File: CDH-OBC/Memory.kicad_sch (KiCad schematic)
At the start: 15 parts, among them U2 MR25H256AMDF, U3 TPS3850H50DRCR, U4 W25N02KVZEIR

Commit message: some progress on kicad
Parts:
- U3: footprint DRC0010J -> OBC-Lib:DRC0010J
- U4: footprint SON_WSON8_ZE_WIN -> OBC-Lib:SON_WSON8_ZE_WIN
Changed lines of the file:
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@@
 			)
 		)
-		(property "Footprint" "DRC0010J"
+		(property "Footprint" "OBC-Lib:DRC0010J"
 			(at 144.78 50.8 0)
 			(hide yes)
@@
 			)
 		)
-		(property "Footprint" "SON_WSON8_ZE_WIN"
+		(property "Footprint" "OBC-Lib:SON_WSON8_ZE_WIN"
 			(at 20.32 95.25 0)
 			(hide yes)

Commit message: changes on rtc
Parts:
- added 1: TL3315NF250Q, symbol OBC-lib:TL3315NF250Q
- added C7: 6.8uF, Capacitor_SMD:C_0603_1608Metric, symbol Device:C_Small
- added C8: 100nF, Capacitor_SMD:C_0603_1608Metric, symbol Device:C_Small
- added C9: 1nF, Capacitor_SMD:C_0603_1608Metric, symbol Device:C_Small
- added R6, R7: 10k, Resistor_SMD:R_0603_1608Metric, symbol Device:R_Small_US
- added U5: PCA2129T/Q900/2_51, SO16_SOT162-1_NXP, symbol OBC-lib:PCA2129T_Q900_2_51
- U3: footprint OBC-Lib:DRC0010J -> DRC0010J
- U4: footprint OBC-Lib:SON_WSON8_ZE_WIN -> SON_WSON8_ZE_WIN
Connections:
- net +3V3: now also C7.2, C8.2, R6.2, U5.16 (VDD)
- net GND: now also C7.1, C8.1, C9.2, U5.15 (VBAT), U5.5 (IFS), U5.8 (VSS)
- new net: R6.1, U5.13 (*INT)
- new net: C9.1, U5.6 (*TS)
- new net: 1.1, 1.2
- new net: 1.3, 1.4

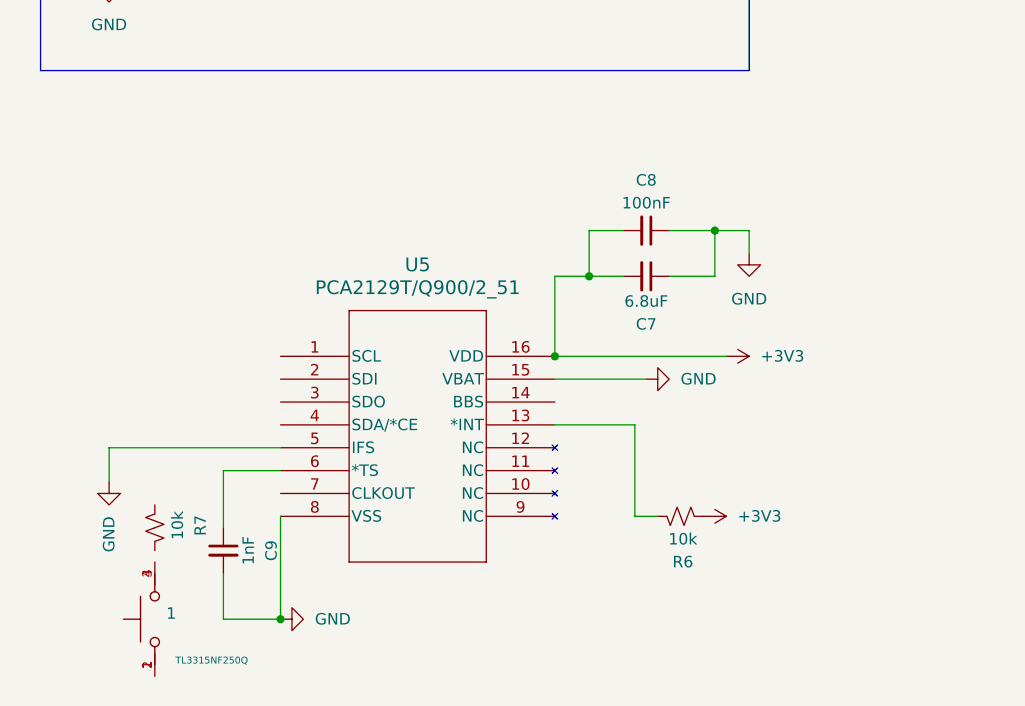
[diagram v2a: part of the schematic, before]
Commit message: changes on mcu and cristal oscillator
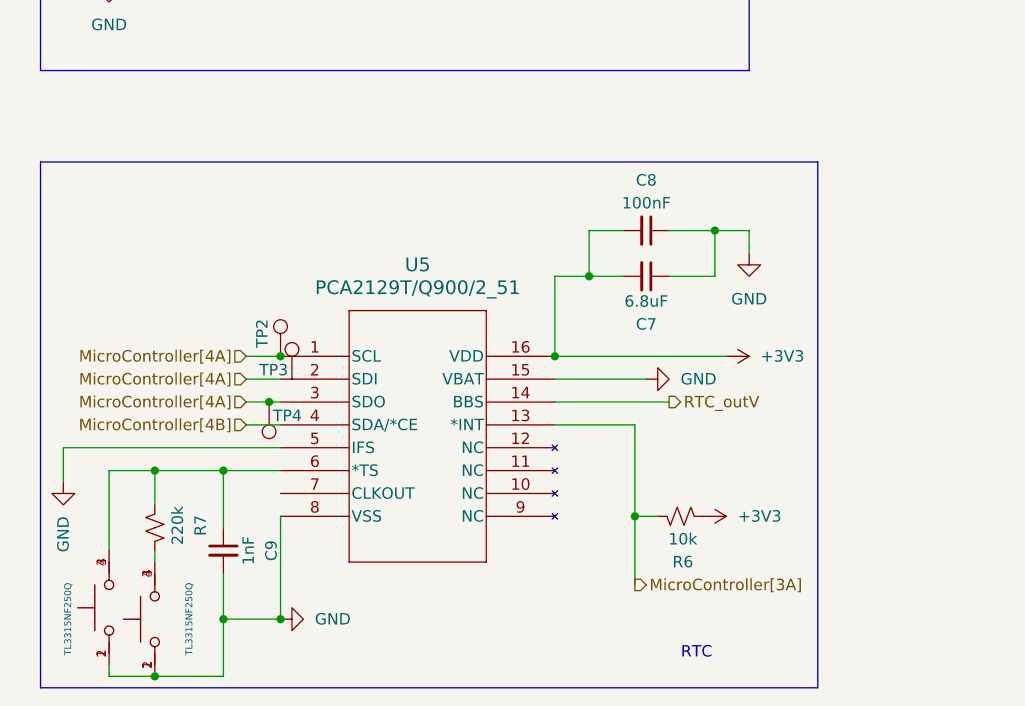
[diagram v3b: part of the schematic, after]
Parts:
- added 11: TL3315NF250Q, symbol OBC-lib:TL3315NF250Q
- added TP2, TP3, TP4: TestPoint, TestPoint:TestPoint_Pad_D1.0mm, symbol Connector:TestPoint
- R7: value 10k -> 220k
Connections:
- net GND: now also 1.1, 1.2, 11.1, 11.2
- net MicroController[3A]: now reaches R6.1, U5.13 (*INT)
- net at C9.1, U5.6 (*TS): now also R7.2, 11.3, 11.4
- net MicroController[4A]: now reaches U5.1 (SCL)
- net MicroController[4A]: now also U5.2 (SDI), U5.3 (SDO), TP2.1, TP4.1
- net RTC_outV: now reaches U5.14 (BBS)
- net MicroController[4B]: now reaches U5.4 (SDA/*CE)
- net at R7.1: now also 1.3, 1.4
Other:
- note added: "RTC"
